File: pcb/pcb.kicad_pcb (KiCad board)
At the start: 2 copper layers, 43.2 x 134 mm, 52 parts, among them J1 Barrel_Jack_Switch, J2 Conn_01x06_Pin, J3 Conn_01x03_Pin, J4 Conn_01x06_Pin, J5 Conn_01x03_Pin, Q1 RQ5P010SN, Q2 IRLML6244, SW1 SW_SPST, SW2 SW_SPST, SW3 SW_SPST, U1 L7805, U2 MCP1406/07, U3 MAX6921AWI, U4 MCP7940N-xSN, U5 Pico, Y1 32.768KHZ

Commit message: new pcb design
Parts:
- removed J4: Conn_01x06_Pin, Connector_PinHeader_2.54mm:PinHeader_1x06_P2.54mm_Horizontal
- removed J5: Conn_01x03_Pin, Connector_PinHeader_2.54mm:PinHeader_1x03_P2.54mm_Horizontal
- J2: value Conn_01x06_Pin -> Conn_02x05_Odd_Even; footprint Connector_PinHeader_2.54mm:PinHeader_1x06_P2.54mm_Vertical -> Connector_PinSocket_2.54mm:PinSocket_2x05_P2.54mm_Vertical
- J3: value Conn_01x03_Pin -> Conn_02x05_Odd_Even; footprint Connector_PinHeader_2.54mm:PinHeader_1x03_P2.54mm_Vertical -> Connector_PinSocket_2.54mm:PinSocket_2x05_P2.54mm_Vertical
- moved J3 65.5 mm to (115.6, 158.8)
- moved SW3 51.6 mm to (149.8, 158.7), turned to -90 degrees
- moved SW2 39.9 mm to (149.8, 147.9), turned to -90 degrees
- moved SW1 38.2 mm to (149.8, 137.1), turned to -90 degrees
- moved TP7 36.1 mm to (115.6, 154.9), turned to 0 degrees
- moved C11 26.7 mm to (132.6, 127.5)
- moved C13 26.7 mm to (141.0, 120.0)
- moved R5 26.7 mm to (133.7, 112.8)
- moved U4 26.7 mm to (132.8, 123.0)
- moved R4 26.7 mm to (133.8, 115.3)
- moved R6 26.7 mm to (133.8, 117.9)
- moved C12 26.7 mm to (141.0, 126.1)
- moved Y1 26.7 mm to (140.4, 124.0)
- moved BT1 24.1 mm to (119.2, 135.9), turned to 90 degrees
- moved TP8 19.4 mm to (120.7, 168.3), turned to 0 degrees
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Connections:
- J2 pad 1: /BLANK -> +3.3V
- J2 pad 2: /LATCH -> /CLOCK
- J2 pad 3: /DATA -> +5V
- J2 pad 4: /CLOCK -> /DATA
- J2 pad 5: /BOOST -> GND
- J2 pad 6: /FIL -> /LATCH
- J3 pad 1: +3.3V -> +3.3VA
- J3 pad 2: GND -> /MCU_CLOCK
- J3 pad 3: +5V -> +5VA
- U5 pad 22: unconnected-(U5-GPIO17-Pad22) -> /MCU_BOOST
- U5 pad 29: /MCU_BOOST -> unconnected-(U5-GPIO22-Pad29)
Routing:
- net /SWITCH3: track 15.4 -> 65.9 mm
- net /SWITCH2: track 17.7 -> 55.1 mm
- net /MCU_CLOCK: track 43.9 -> 70.0 mm
- net +5VA: track 73.8 -> 48.5 mm
- net /MFP: track 7.30 -> 32.6 mm
- net /SCL: track 9.25 -> 32.9 mm
- net /SDA: track 9.68 -> 32.0 mm
- net /MCU_BOOST: track 31.1 -> 9.13 mm
- net /SWITCH1: track 22.7 -> 43.2 mm
- net /MCU_DATA: track 41.4 -> 61.8 mm
- net /MCU_LATCH: track 35.8 -> 53.4 mm
- net /BLANK: track 64.9 -> 76.8 mm
- net GNDA: track 19.9 -> 9.64 mm, vias 0 -> 2
- net /MCU_BLANK: track 32.0 -> 40.0 mm
- net +3.3VA: track 85.8 -> 78.2 mm, vias 0 -> 1
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- added copper zone on B.Cu, net (none)
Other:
- board size 43.2 x 134 mm -> 43.2 x 137.2 mm

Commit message: small fixes
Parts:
- D2: value SDT5A60SA-13 -> FM4004-W
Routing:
- net GND: track 17.9 -> 10.2 mm
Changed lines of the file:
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@@
     (property "Sheetfile" "pcb.kicad_sch")
     (property "Sheetname" "")
-    (property "ki_description" "Schottky diode")
-    (property "ki_keywords" "diode Schottky")
+    (property "Sim.Device" "D")
+    (property "Sim.Pins" "1=K 2=A")
+    (property "ki_description" "Diode")
+    (property "ki_keywords" "diode")
     (attr smd)
     (fp_text reference "D2" (at 5.675 0 90) (layer "F.SilkS")
         (effects (font (size 1 1) (thickness 0.15)))
     )
-    (fp_text value "SDT5A60SA-13" (at 0 2.6 90) (layer "F.SilkS")
+    (fp_text value "FM4004-W" (at 0 2.6 90) (layer "F.SilkS")
         (effects (font (size 1 1) (thickness 0.15)))
     )
@@
   (segment (start 131.751976 128.916) (end 132.196 128.471976) (width 0.2032) (layer "F.Cu") (net 1))
   (segment (start 133.816 123.204226) (end 133.816 123.193646) (width 0.2032) (layer "F.Cu") (net 1))
-  (segment (start 125.095 43.053) (end 127.635 40.513) (width 0.6096) (layer "F.Cu") (net 2))
   (segment (start 148.59 81.915) (end 148.54 81.865) (width 0.6096) (layer "F.Cu") (net 2))
-  (segment (start 127.635 40.513) (end 127.635 36.42) (width 0.6096) (layer "F.Cu") (net 2))
   (segment (start 120.534537 67.933462) (end 120.522999 67.945) (width 0.6096) (layer "F.Cu") (net 2))
   (segment (start 120.522999 67.945) (end 118.745 67.945) (width 0.6096) (layer "F.Cu") (net 2))

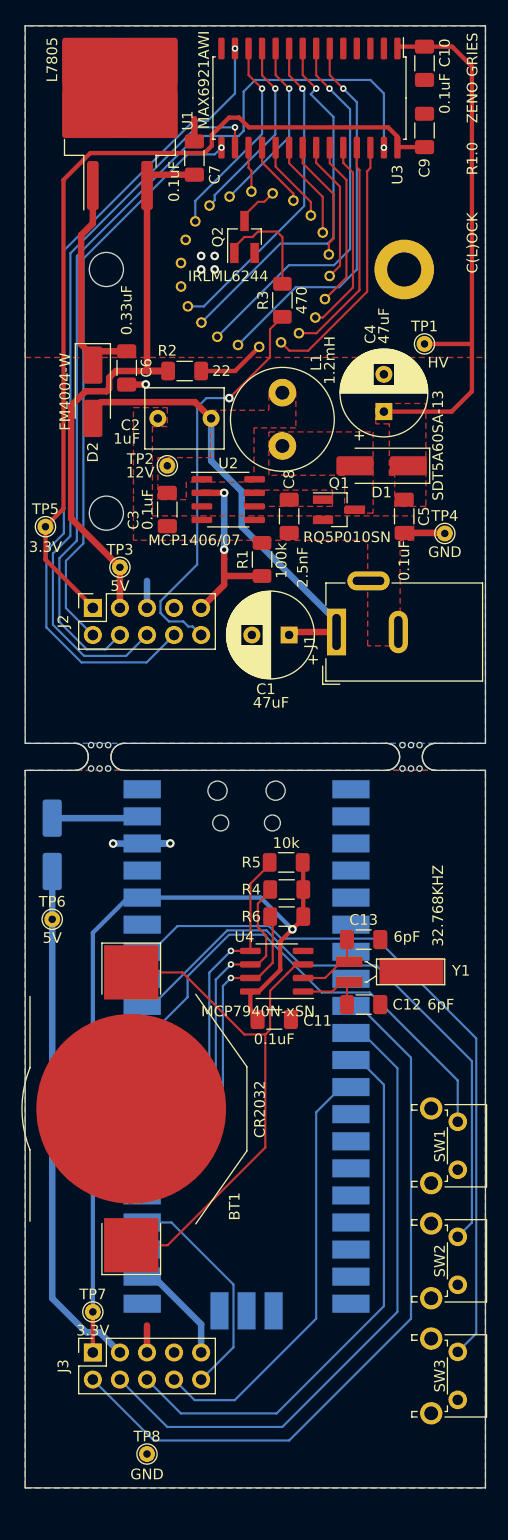
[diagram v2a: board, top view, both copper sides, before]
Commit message: decreased costs
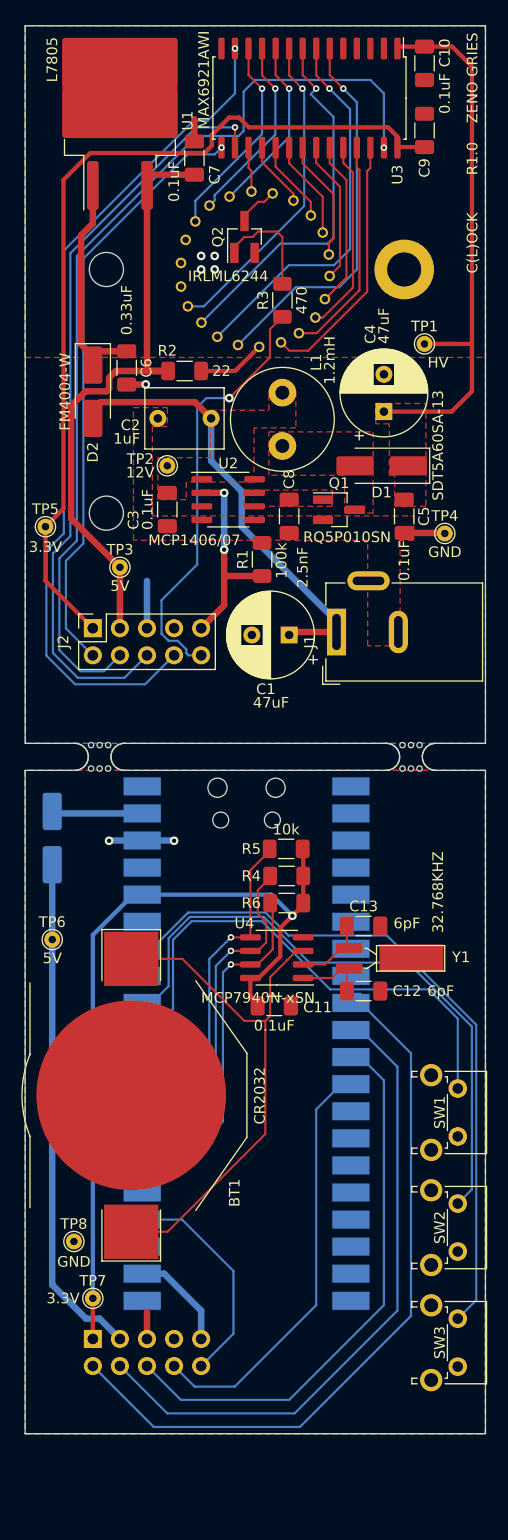
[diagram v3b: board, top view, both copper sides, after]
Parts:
- moved TP8 21.1 mm to (113.8, 148.3)
- moved SW2 3.12 mm to (149.8, 144.8)
- moved SW3 3.12 mm to (149.8, 155.6)
- moved SW1 3.12 mm to (149.8, 134.0)
- moved J2 1.91 mm to (115.6, 90.8)
- moved TP6 1.91 mm to (111.8, 120.0)
- moved C12 1.27 mm to (141.0, 124.8)
- moved J3 1.27 mm to (115.6, 157.5)
- moved TP7 1.27 mm to (115.6, 153.7)
- moved Y1 1.27 mm to (140.4, 122.7)
- moved C11 1.27 mm to (132.6, 126.2)
- moved C13 1.27 mm to (141.0, 118.7)
- moved R4 1.27 mm to (133.8, 114.0)
- moved R5 1.27 mm to (133.7, 111.5)
- moved R6 1.27 mm to (133.8, 116.6)
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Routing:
- net /SWITCH1: track 43.2 -> 47.1 mm
- net /LATCH: track 68.6 -> 71.1 mm
- net /BLANK: track 76.8 -> 79.3 mm
- net /DATA: track 85.7 -> 88.2 mm
- net /SWITCH2: track 55.1 -> 57.4 mm
- net /FIL: track 38.7 -> 40.7 mm
- net GND: track 10.2 -> 12.2 mm
- net /BOOST: track 17.3 -> 19.2 mm
- net +5V: track 56.7 -> 58.6 mm
- net +3.3V: track 81.4 -> 83.3 mm
- net /CLOCK: track 54.3 -> 56.2 mm
- net +3.3VA: track 78.2 -> 76.5 mm
- net /MCU_CLOCK: track 70.0 -> 71.5 mm
- net /SWITCH3: track 65.9 -> 64.5 mm
- net /MCU_BLANK: track 40.0 -> 39.0 mm
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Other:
- board size 43.2 x 137.2 mm -> 43.2 x 132.1 mm
